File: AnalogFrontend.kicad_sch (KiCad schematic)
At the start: 2 parts, among them J1 USB_C_Receptacle_USB2.0_14P, U1 SE5004L

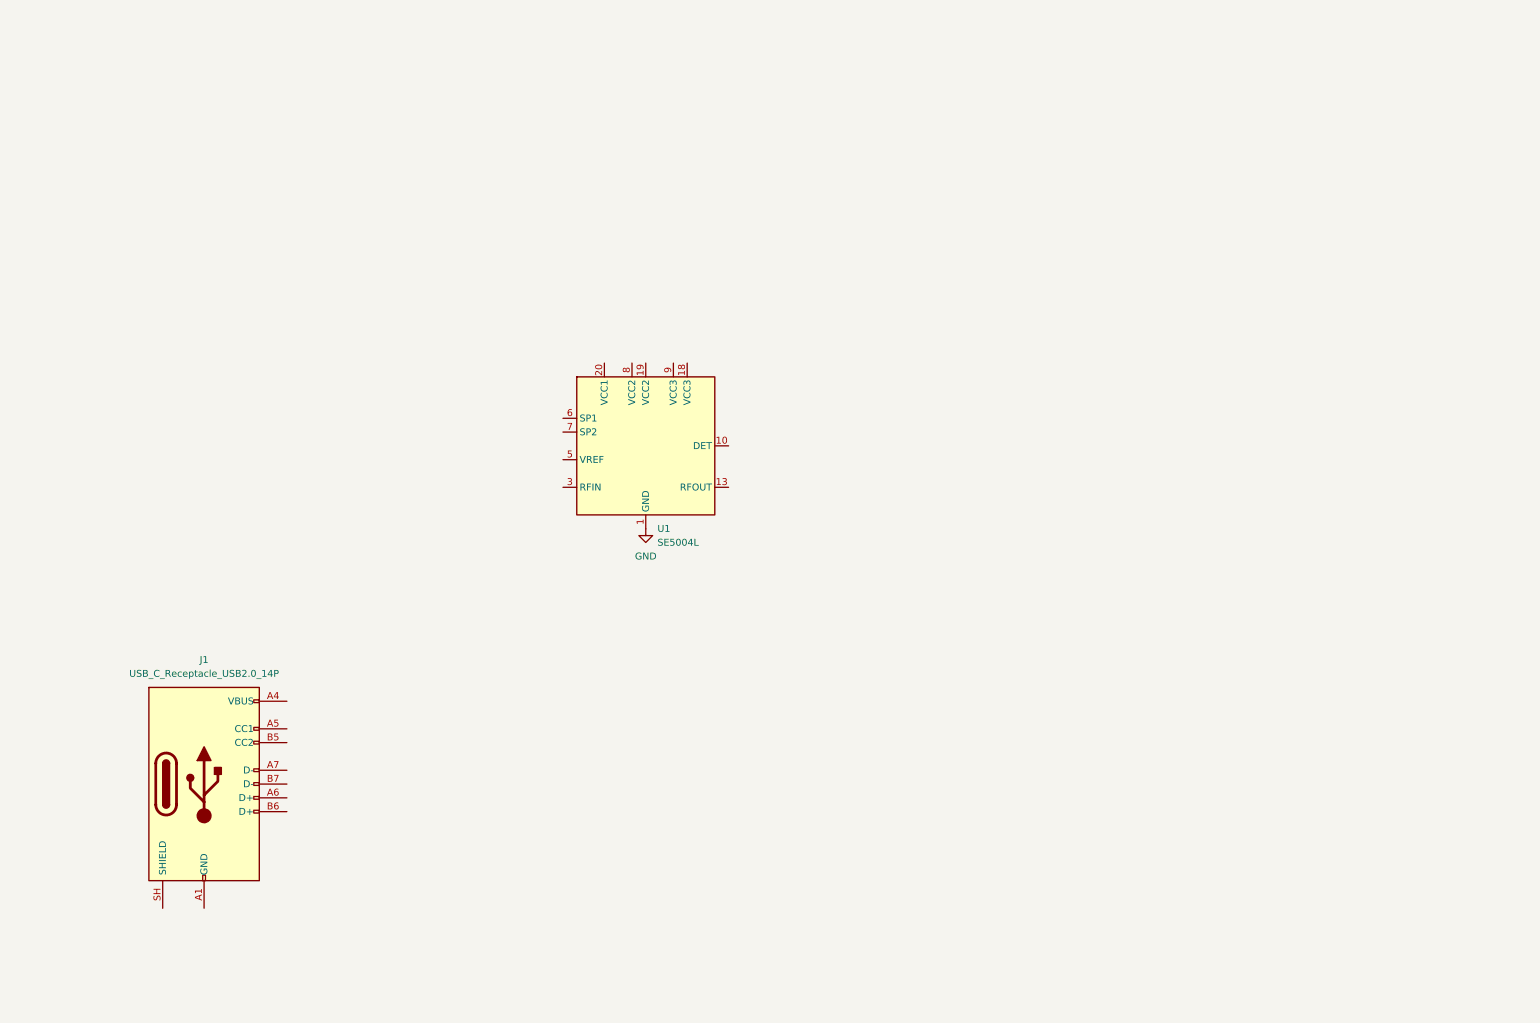
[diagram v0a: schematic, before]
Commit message: update schematic
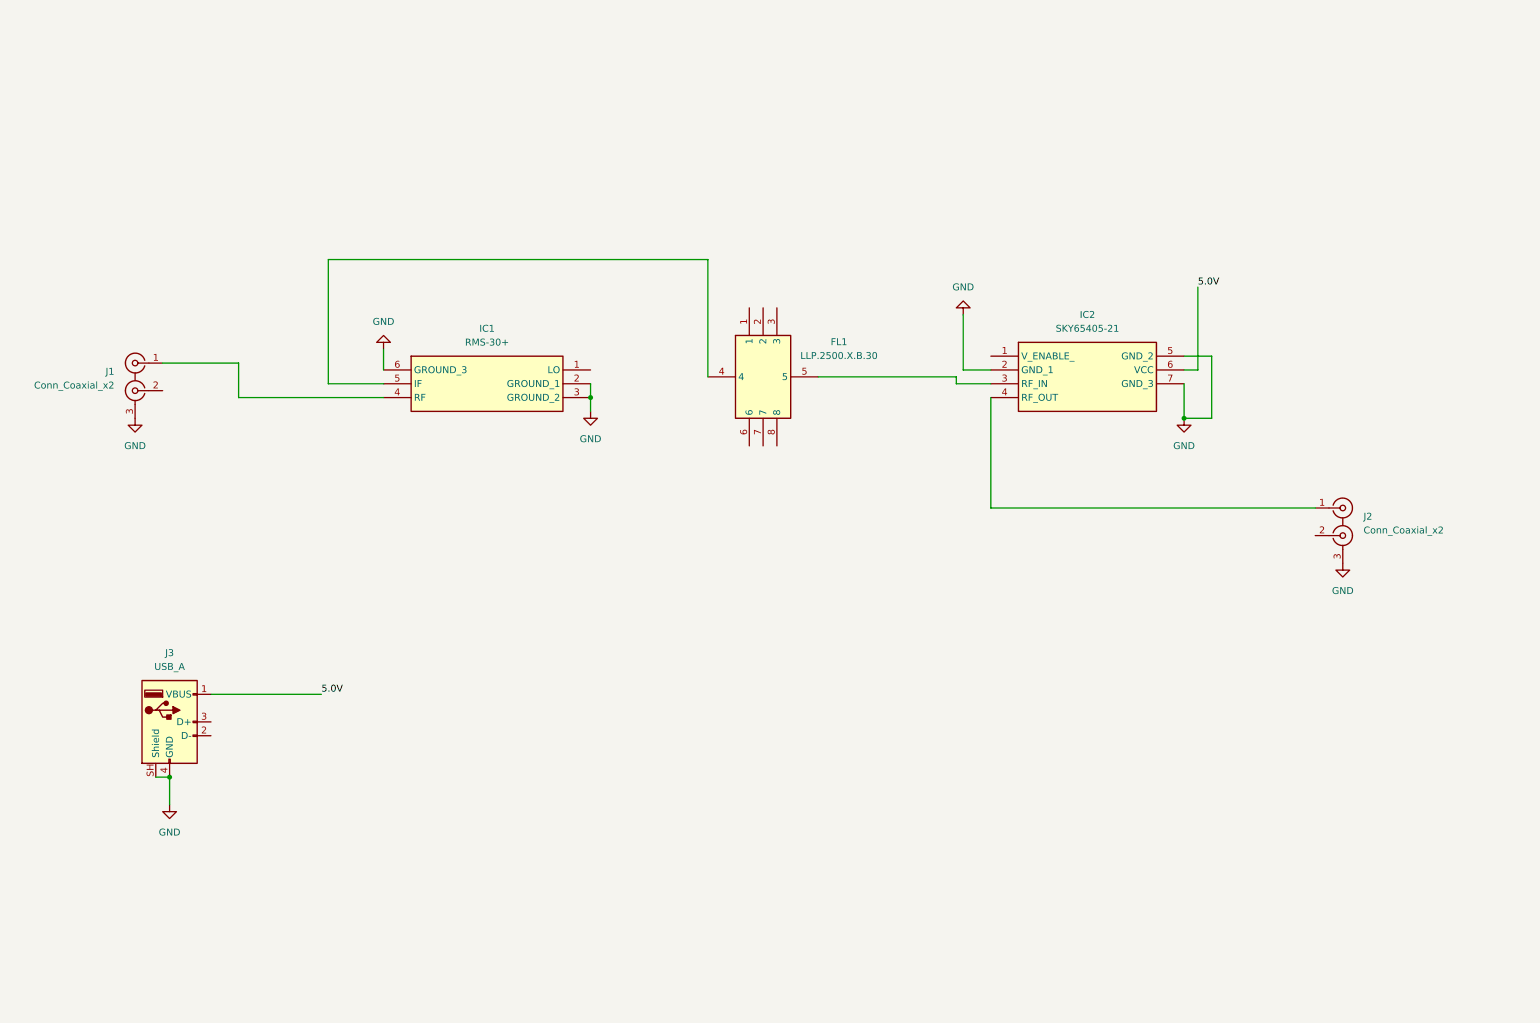
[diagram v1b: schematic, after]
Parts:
- removed J1: USB_C_Receptacle_USB2.0_14P, symbol Connector:USB_C_Receptacle_USB2.0_14P
- removed U1: SE5004L, Package_DFN_QFN:QFN-20-1EP_4x4mm_P0.5mm_EP2.5x2.5mm, symbol RF:SE5004L
- added FL1: LLP.2500.X.B.30, LLP2500XB30, symbol SamacSys_Parts:LLP.2500.X.B.30
- added IC1: RMS-30+, RMS30, symbol SamacSys_Parts:RMS-30+
- added IC2: SKY65405-21, SKY6540521, symbol SamacSys_Parts:SKY65405-21
- added J1, J2: Conn_Coaxial_x2, symbol Connector:Conn_Coaxial_x2
- added J3: USB_A, symbol Connector:USB_A
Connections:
- net GND: now also IC1.2 (GROUND_1), IC1.3 (GROUND_2), IC1.6 (GROUND_3), IC2.2 (GND_1), IC2.5 (GND_2), IC2.7 (GND_3), J1.3 (EXT), J2.3 (EXT), J3.4 (GND), J3.SH (Shield)
- new net: IC1.4 (RF), J1.1 (IN1)
- new net: FL1.4, IC1.5 (IF)
- new net: FL1.5, IC2.3 (RF_IN)
- new net: IC2.4 (RF_OUT), J2.1 (IN1)
- new net 5.0V: IC2.6 (VCC), J3.1 (VBUS)
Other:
- title: (none) -> Transmitter

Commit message: updatged schematics
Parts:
- removed IC2: SKY65405-21, SKY6540521, symbol SamacSys_Parts:SKY65405-21
- added C4, C5, C6: 4.7muF, Capacitor_SMD:C_1206_3216Metric_Pad1.33x1.80mm_HandSolder, symbol Device:C
- added D1: LED, symbol Device:LED
- added IC4: SE2576L-R, SamacSys_Parts:QFN50P300X300X90-17N-D, symbol SamacSys_Parts:SE2576L-R
- added J7: Conn_01x01_Pin, symbol Connector:Conn_01x01_Pin
- added R1: R, Resistor_SMD:R_0612_1632Metric_Pad1.18x3.40mm_HandSolder, symbol Device:R
- added R3: 200k, Resistor_SMD:R_0612_1632Metric_Pad1.18x3.40mm_HandSolder, symbol Device:R
- added R4: 33.2k, Resistor_SMD:R_0612_1632Metric_Pad1.18x3.40mm_HandSolder, symbol Device:R
- added R5: 499, Resistor_SMD:R_0612_1632Metric_Pad1.18x3.40mm_HandSolder, symbol Device:R
- added R6: 453k, Resistor_SMD:R_0612_1632Metric_Pad1.18x3.40mm_HandSolder, symbol Device:R
- added R7: 49.9k, Resistor_SMD:R_0612_1632Metric_Pad1.18x3.40mm_HandSolder, symbol Device:R
- added U2: LT3042xMSE, Package_SO:MSOP-10-1EP_3x3mm_P0.5mm_EP1.68x1.88mm, symbol Regulator_Linear:LT3042xMSE
- FL1: footprint LLP2500XB30 -> SamacSys_Parts:LLP2500XB30
- IC1: footprint RMS30 -> SamacSys_Parts:RMS30
- J3: footprint (none) -> Connector_USB:USB3_A_Molex_48393-001
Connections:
- net GND: now also FL1.1, FL1.2, FL1.3, FL1.6, FL1.7, FL1.8, C4.2, C5.2, C6.2, IC4.12 (GND_5), IC4.16 (GND_6), IC4.17 (EP_(GND)), IC4.3 (GND_1), IC4.5 (GND_2), IC4.6 (GND_3), IC4.8 (NC_1), IC4.9 (GND_4), R1.2, R4.1, R5.1, R7.1, U2.11 (GND), U2.8 (GND)
- net at J1.1 (IN1): now also IC1.5 (IF); no longer IC1.4 (RF)
- net at FL1.4: now also IC1.4 (RF); no longer IC1.5 (IF)
- net at FL1.5: now also IC4.1 (RF_IN)
- net Oscillator TX Output: now reaches IC1.1 (LO)
- net at J2.1 (IN1): now also IC4.10 (RFOUT), IC4.11 (RF_OUT)
- net 5.0V renamed +5V
- net +5V: now also C4.1, D1.2 (A), IC4.13 (VCC2), IC4.15 (VCC1), IC4.2 (EN), IC4.4 (VCCO), R3.1, U2.1 (IN), U2.2 (IN), U2.3 (EN/UV)
- new net: IC4.7 (DET), J7.1 (Pin_1)
- new net: R6.1, R7.2, U2.6 (PGFB)
- new net: D1.1 (K), R1.1
- new net: R3.2, U2.4 (PG)
- new net: R5.2, U2.5 (ILIM)
- new net: C5.1, R4.2, U2.7 (SET)
- new net +3.3V: C6.1, R6.2, U2.10 (OUT), U2.9 (OUTS)
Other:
- moved on the sheet: FL1, IC1, J1, J2, J3

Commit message: updated schematics
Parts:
- J1, J2: footprint (none) -> Connector_Coaxial:SMA_Amphenol_132289_EdgeMount
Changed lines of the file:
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@@
 			)
 		)
-		(property "Footprint" ""
+		(property "Footprint" "Connector_Coaxial:SMA_Amphenol_132289_EdgeMount"
 			(at 34.29 26.67 0)
 			(hide yes)
@@
 			)
 		)
-		(property "Footprint" ""
+		(property "Footprint" "Connector_Coaxial:SMA_Amphenol_132289_EdgeMount"
 			(at 266.7 62.23 0)
 			(hide yes)
